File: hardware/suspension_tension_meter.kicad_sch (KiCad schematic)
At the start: 15 parts, among them J1 I2C, U1 STM32L4P5RET6, Y1 TBD

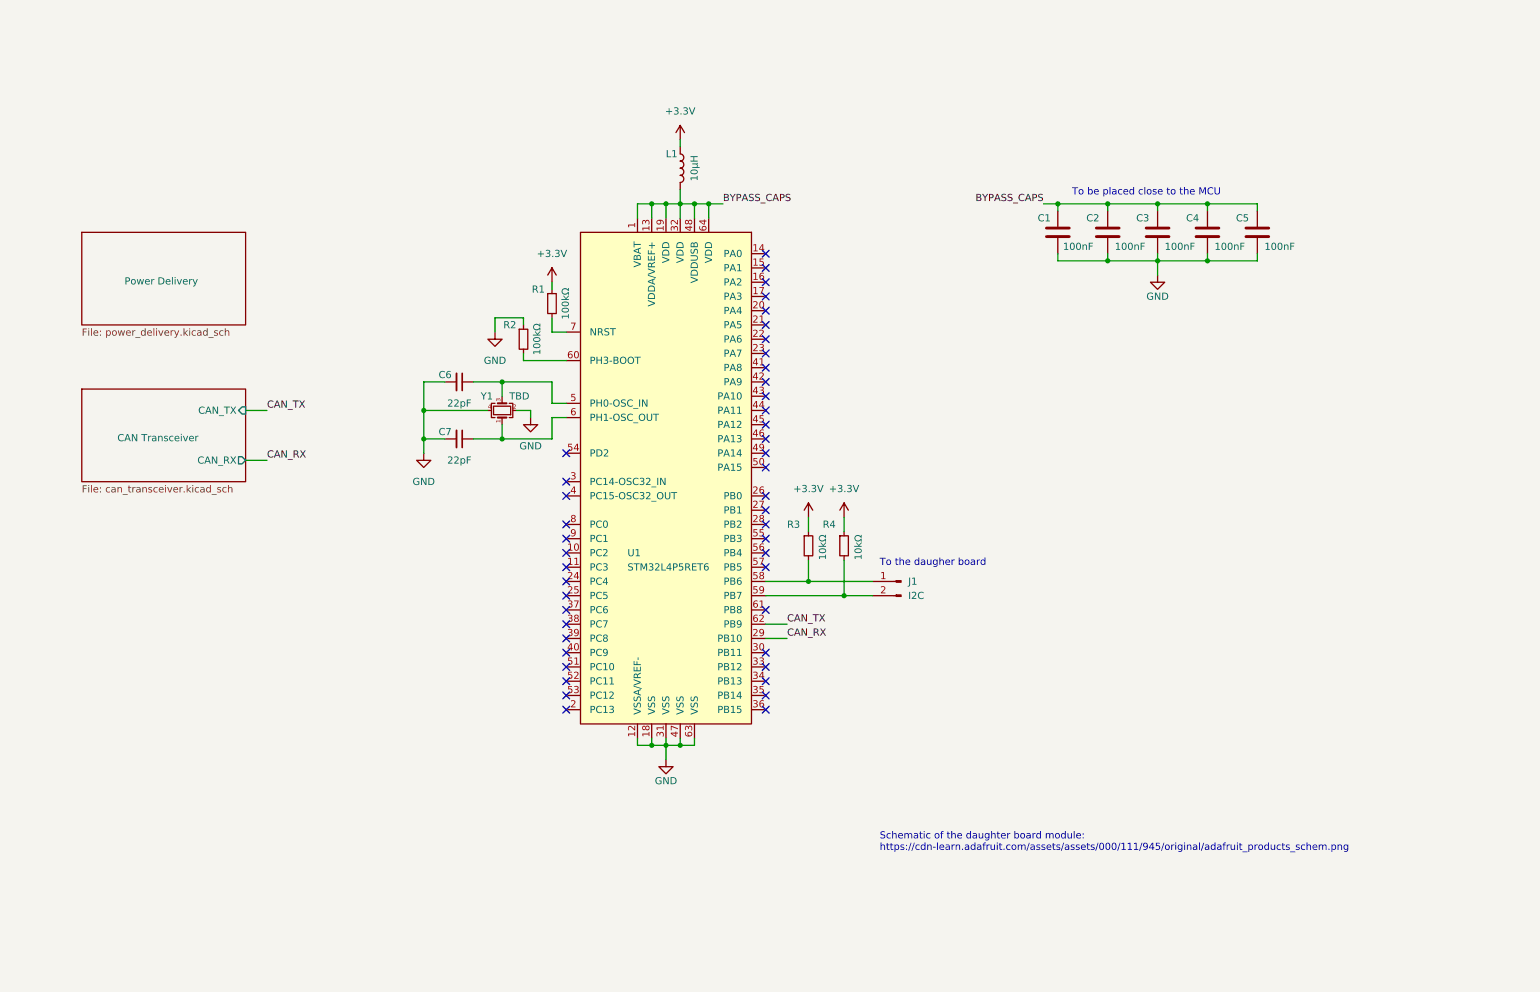
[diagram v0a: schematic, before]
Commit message: Improve the CAN transceiver circuit
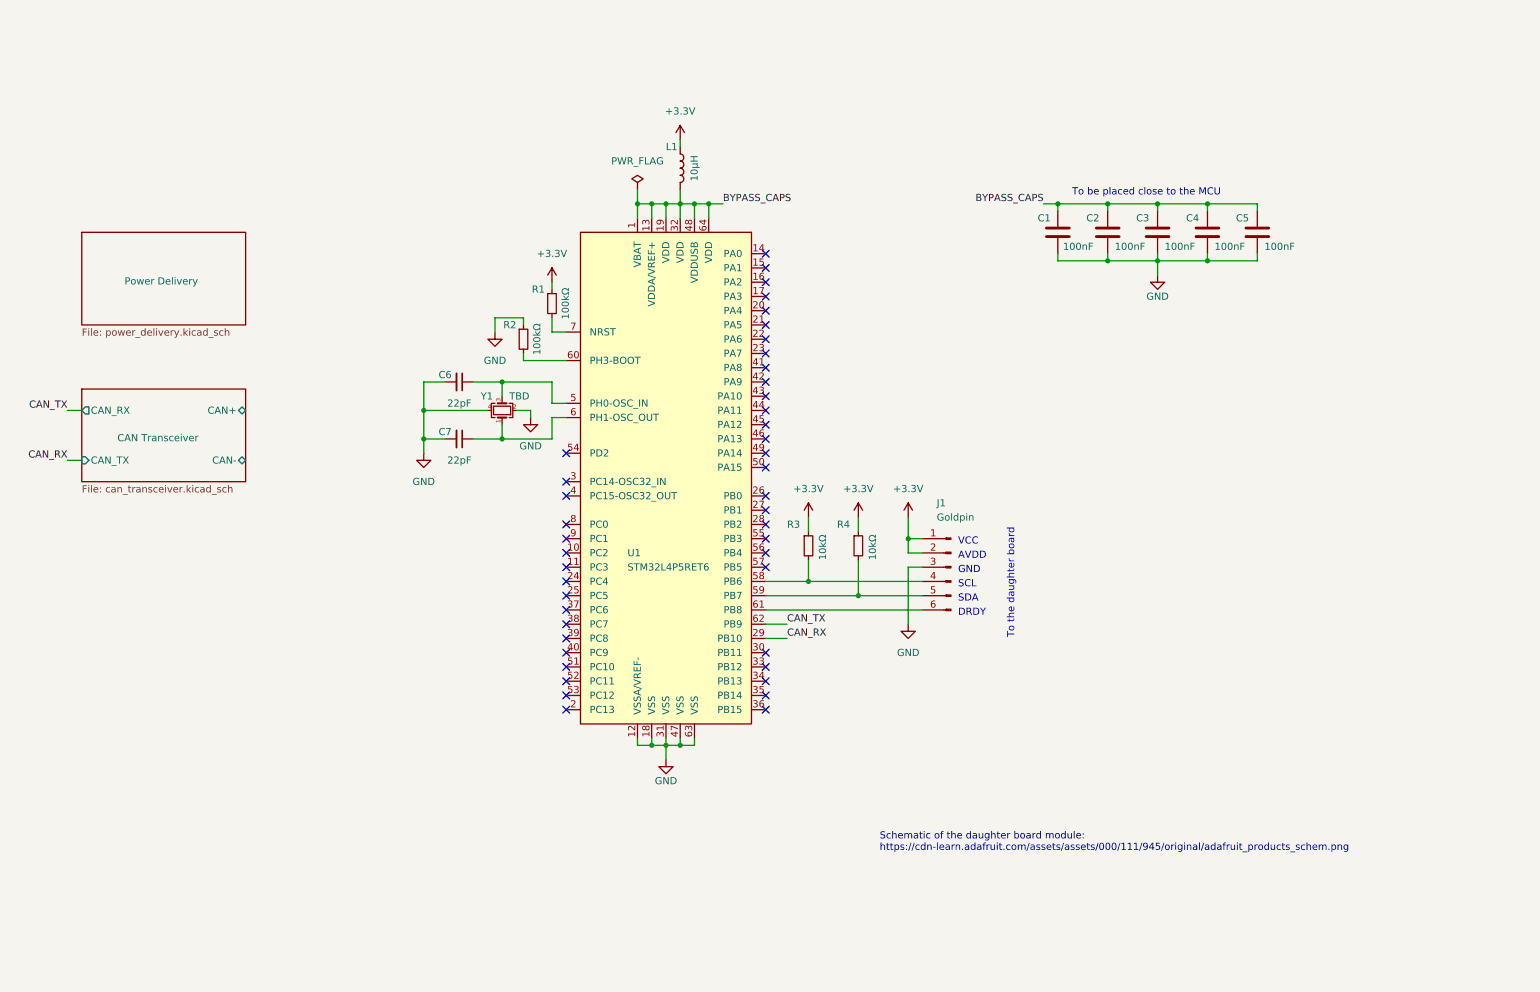
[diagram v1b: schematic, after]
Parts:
- removed J1: I2C, symbol Connector:Conn_01x02_Male
- added J1: Goldpin, symbol Connector:Conn_01x06_Male
- U1: symbol PUTM:STM32L4P5RET6 -> Local_Library:STM32L4P5RET6-STM32L4P5RET6
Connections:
- net +3.3V: now also J1.1 (Pin_1), J1.2 (Pin_2)
- net GND: now also J1.3 (Pin_3)
- net at R3.2, U1.58 (PB6): now also J1.4 (Pin_4)
- net at R4.2, U1.59 (PB7): now also J1.5 (Pin_5)
- net at U1.61 (PB8): now also J1.6 (Pin_6)
- no-connect marks 45 -> 44
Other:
- sheet CAN Transceiver ports: added CAN+, CAN-; removed none
- note added: "AVDD"
- note added: "DRDY"
- note added: "GND"
- note added: "SCL"
- note added: "SDA"
- note added: "To the daughter board"
- note added: "VCC"
- note removed: "To the daugher board"
- company: PUT MotorSport -> PUT Motorsport
- moved on the sheet: R4

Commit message: Add a low-pass filter to the analog circuit supply
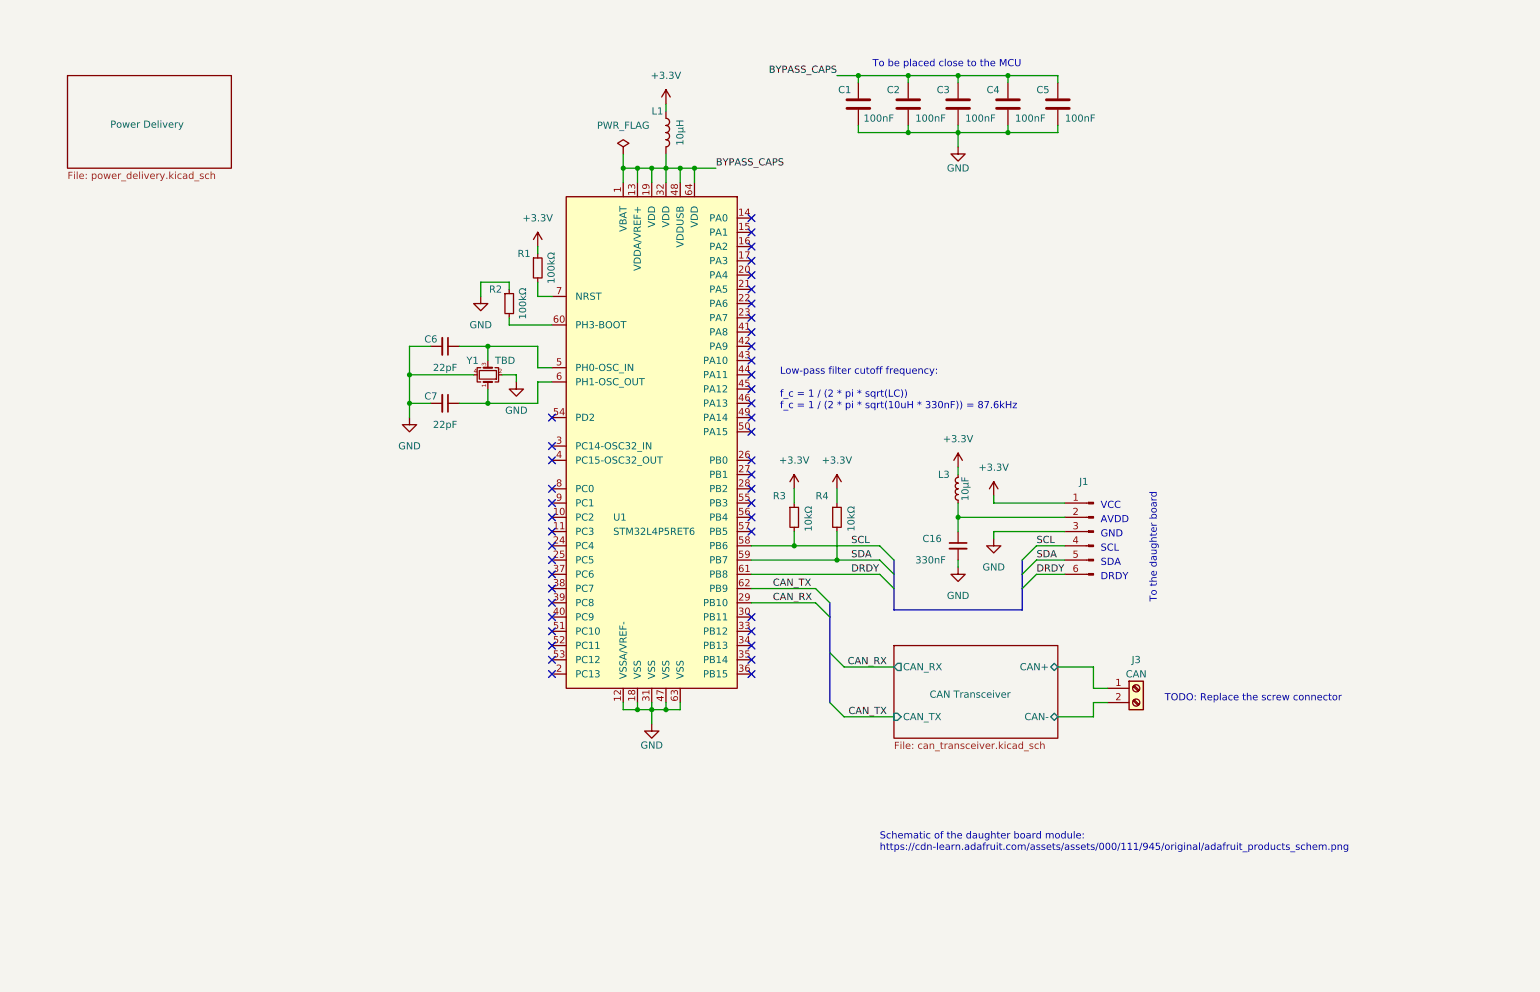
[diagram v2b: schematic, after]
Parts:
- added C16: 330nF, symbol Device:C_Small
- added J3: CAN, symbol Connector:Screw_Terminal_01x02
- added L3: 10μF, symbol Device:L_Small
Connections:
- net +3.3V: now also L3.2; no longer J1.2 (Pin_2)
- net CAN Transceiver/CAN+: now also J3.1 (Pin_1)
- net CAN Transceiver/CAN-: now also J3.2 (Pin_2)
- net GND: now also C16.2
- net SCL: now reaches J1.4 (Pin_4), R3.2, U1.58 (PB6)
- net SDA: now reaches J1.5 (Pin_5), R4.2, U1.59 (PB7)
- net DRDY: now reaches J1.6 (Pin_6), U1.61 (PB8)
- new net: C16.1, J1.2 (Pin_2), L3.1
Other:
- note added: "Low-pass filter cutoff frequency: f_c = 1 / (2 * pi * sqrt(LC)) f_c = 1 / (2 * pi * sqrt(10uH * 330nF)) = 87.6kHz"
- note added: "TODO: Replace the screw connector"
- moved on the sheet: C1, C2, C3, C4, C5, C6, C7, J1, L1, R1, R2, R3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

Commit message: Improve power delivery sheet:
- Move power connector to the main sheet
- Use PTC fuse
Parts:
- added J2: 24V, symbol Connector:Screw_Terminal_01x02
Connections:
- new net Power Delivery/PWR+: J2.1 (Pin_1)
- new net Power Delivery/PWR-: J2.2 (Pin_2)
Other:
- sheet Power Delivery ports: added PWR+, PWR-; removed none
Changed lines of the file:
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@@
+    (stroke (width 0) (type default) (color 0 0 0 0))
+  )
+  (wire (pts (xy 38.1 40.64) (xy 40.64 40.64))
     (stroke (width 0) (type default) (color 0 0 0 0))
   )
@@
     (stroke (width 0) (type default) (color 0 0 0 0))
   )
+  (wire (pts (xy 40.64 43.18) (xy 38.1 43.18))
+    (stroke (width 0) (type default) (color 0 0 0 0))
+  )
   (wire (pts (xy 132.08 46.99) (xy 132.08 49.53))
     (stroke (width 0) (type default) (color 0 0 0 0))
@@
     (stroke (width 0) (type default) (color 0 0 0 0))
   )
+  (wire (pts (xy 40.64 45.72) (xy 40.64 43.18))
+    (stroke (width 0) (type default) (color 0 0 0 0))
+  )
   (wire (pts (xy 198.12 109.22) (xy 198.12 107.95))
     (stroke (width 0) (type default) (color 0 0 0 0))
@@
     (stroke (width 0) (type default) (color 0 0 0 0))
   )
+  (wire (pts (xy 40.64 36.83) (xy 43.18 36.83))
+    (stroke (width 0) (type default) (color 0 0 0 0))
+  )
   (wire (pts (xy 111.76 77.47) (xy 119.38 77.47))
     (stroke (width 0) (type default) (color 0 0 0 0))
@@
     (stroke (width 0) (type default) (color 0 0 0 0))
   )
+  (wire (pts (xy 40.64 40.64) (xy 40.64 36.83))
+    (stroke (width 0) (type default) (color 0 0 0 0))
+  )
   (wire (pts (xy 154.94 116.84) (xy 162.56 116.84))
     (stroke (width 0) (type default) (color 0 0 0 0))
@@
   )
   (wire (pts (xy 132.08 146.05) (xy 134.62 146.05))
+    (stroke (width 0) (type default) (color 0 0 0 0))
+  )
+  (wire (pts (xy 43.18 45.72) (xy 40.64 45.72))
     (stroke (width 0) (type default) (color 0 0 0 0))
   )
@@
     (pin "5")
     (pin "6")
+  )
+  (symbol (lib_id "Connector:Screw_Terminal_01x02") (at 33.02 40.64 0) (mirror y) (unit 1)
+    (in_bom yes) (on_board yes)
+    (property "Reference" "J2" (id 0) (at 33.02 35.56 0))
+    (property "Value" "24V" (id 1) (at 33.02 38.1 0))
+    (property "Footprint" "" (id 2) (at 33.02 40.64 0)
+      (effects (font (size 1.27 1.27)) hide)
+    )
+    (property "Datasheet" "~" (id 3) (at 33.02 40.64 0)
+      (effects (font (size 1.27 1.27)) hide)
+    )
+    (pin "1")
+    (pin "2")
   )
   (symbol (lib_id "Device:L") (at 139.7 43.18 0) (unit 1)
@@
     )
   )
-  (sheet (at 33.02 33.02) (size 29.21 16.51)
+  (sheet (at 43.18 33.02) (size 29.21 16.51)
     (stroke (width 0.1524) (type solid) (color 0 0 0 0))
     (fill (color 0 0 0 0.0000))
-    (property "Sheet name" "Power Delivery" (id 0) (at 40.64 42.4684 0)
+    (property "Sheet name" "Power Delivery" (id 0) (at 50.8 42.4684 0)
       (effects (font (size 1.27 1.27)) (justify left bottom))
     )
-    (property "Sheet file" "power_delivery.kicad_sch" (id 1) (at 33.02 50.1146 0)
+    (property "Sheet file" "power_delivery.kicad_sch" (id 1) (at 43.18 51.3846 0)
       (effects (font (size 1.27 1.27)) (justify left top))
+    )
+    (pin "PWR-" input (at 43.18 45.72 180)
+      (effects (font (size 1.27 1.27)) (justify left))
+    )
+    (pin "PWR+" input (at 43.18 36.83 180)
+      (effects (font (size 1.27 1.27)) (justify left))
     )
   )
@@
       (reference "D2") (unit 1) (value "PESD2CAN.215") (footprint "Package_TO_SOT_SMD:SOT-23")
     )
-    (path "/806827ee-9314-4e25-8483-d67eef20445a/a4d95e9c-6f0a-4fbe-98e6-8c71c04c235f"
-      (reference "F1") (unit 1) (value "100mA") (footprint "")
+    (path "/806827ee-9314-4e25-8483-d67eef20445a/8a6e2d34-b551-475d-be1b-b9e252f573ef"
+      (reference "F1") (unit 1) (value "500mA") (footprint "")
     )
     (path "/5e14743a-2b2f-4bbb-8a38-9e15eddfe6cc/c89e316a-f345-4ecb-b95d-d9f2f45fb2d6"
@@
       (reference "J1") (unit 1) (value "Goldpin") (footprint "")
     )
-    (path "/806827ee-9314-4e25-8483-d67eef20445a/6cf74833-1188-4dcf-8b6b-9dcf7b62800b"
+    (path "/696ffe04-8b8c-4b0a-965f-f01e29ab1e88"
       (reference "J2") (unit 1) (value "24V") (footprint "")
     )
